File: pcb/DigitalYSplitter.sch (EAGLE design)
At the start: 42 parts, among them CN1 Battery, CON1 USB_MICROSMT+THRUHULE, CON2 M05X2NO_SILK, CON3 LED_OUT, CON5 LED_OUT, Q1 16MHz, SW1 BUTTON_1, SW2 BUTTON_2, U1 MK20D--VFM5, U3 74LVC1G17DCK, U4 74LVC1G17DCK, U5 74LVC1G17DCK, U6 TPD4S012, U7 74LVC1G17DCK

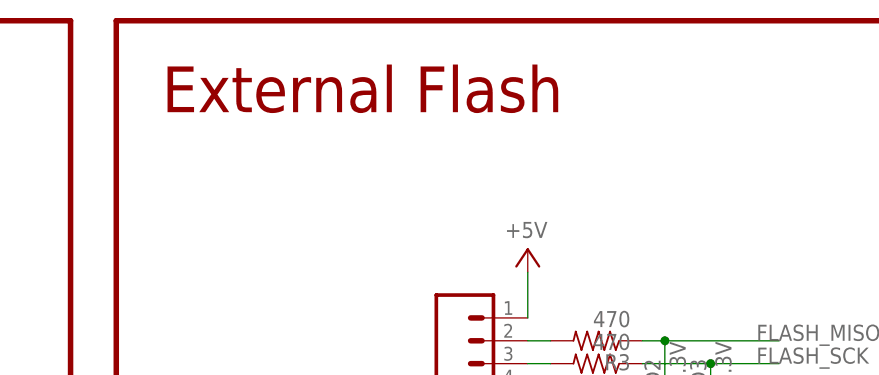
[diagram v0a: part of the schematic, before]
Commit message: Rename files, add .gitignore
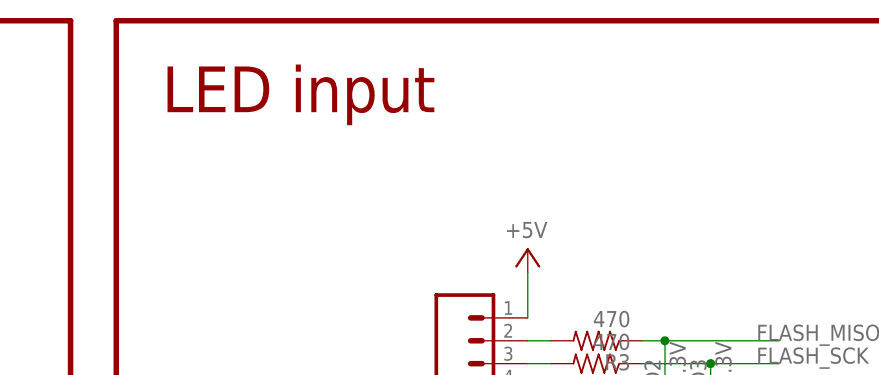
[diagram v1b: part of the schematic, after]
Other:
- note added: "LED input"
- note removed: "External Flash"
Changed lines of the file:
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@@
 <text x="20.32" y="238.76" size="5.08" layer="94">Processor</text>
 <wire x1="256.54" y1="248.92" x2="345.44" y2="248.92" width="0.6096" layer="94"/>
-<text x="261.62" y="238.76" size="5.08" layer="94">External Flash</text>
+<text x="261.62" y="238.76" size="5.08" layer="94">LED input</text>
 <wire x1="256.54" y1="248.92" x2="256.54" y2="165.1" width="0.6096" layer="94"/>
 <wire x1="345.44" y1="248.92" x2="345.44" y2="165.1" width="0.6096" layer="94"/>

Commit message: Small corrections to the PCB
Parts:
- removed LED5: STATUS, adafruit:LEDCHIPLED_0805
- removed R4: 470, adafruit:R-US_R0402
- renumbered LED6 to LED0
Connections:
- removed net N$16: LED1.A, R4.1
- removed net POWER_ENABLE: U1.PTD4
- removed net STATUS: LED1.C, U1.PTD6
- net +3V3: no longer R4.2
- net N$17: now also LED1.A; no longer LED5.A
- net TX: now also LED1.C; no longer LED5.C
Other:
- note removed: "Design Note: Signals POWER_ENABLE, STATUS, SW2, SW1 are GPIO and can be swapped to any other pin besides the ones on Port C"
- note removed: "Design Note: This is a generic flash pinout, there are equivalent parts from Winbond, Spansion, etc. Use the hardware chip select function to avoid conflicting with the LED output DMA."
- moved on the sheet: LED1
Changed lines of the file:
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@@
 <part name="GND10" library="SparkFun-Aesthetics" deviceset="GND" device=""/>
 <part name="C1" library="adafruit" deviceset="C-US" device="C0402" value="100nF"/>
-<part name="R4" library="adafruit" deviceset="R-US_" device="R0402" value="470"/>
-<part name="LED1" library="adafruit" deviceset="LED" device="CHIPLED_0805" value="STATUS"/>
 <part name="GND12" library="supply1" deviceset="GND" device=""/>
-<part name="3V3" library="supply1" deviceset="+3V3" device=""/>
 <part name="P+9" library="supply1" deviceset="+5V" device=""/>
 <part name="C3" library="adafruit" deviceset="C-US" device="C0402" value="100nF"/>
@@
 <part name="3V5" library="supply1" deviceset="+3V3" device=""/>
 <part name="R9" library="adafruit" deviceset="R-US_" device="R0402" value="470"/>
-<part name="LED5" library="adafruit" deviceset="LED" device="CHIPLED_0805" value="STATUS"/>
+<part name="LED1" library="adafruit" deviceset="LED" device="CHIPLED_0805" value="STATUS"/>
 <part name="3V6" library="supply1" deviceset="+3V3" device=""/>
 <part name="R10" library="adafruit" deviceset="R-US_" device="R0402" value="470"/>
-<part name="LED6" library="adafruit" deviceset="LED" device="CHIPLED_0805" value="STATUS"/>
+<part name="LED0" library="adafruit" deviceset="LED" device="CHIPLED_0805" value="STATUS"/>
 <part name="3V7" library="supply1" deviceset="+3V3" device=""/>
 </parts>
@@
 <wire x1="251.46" y1="124.46" x2="251.46" y2="40.64" width="0.6096" layer="94"/>
 <text x="20.32" y="114.3" size="5.08" layer="94">Buttons</text>
-<text x="165.1" y="134.62" size="1.778" layer="91">Design Note:
-Signals POWER_ENABLE, STATUS, SW2, SW1
-are GPIO and can be swapped to any other
-pin besides the ones on Port C</text>
 <text x="22.86" y="132.08" size="1.778" layer="91">Design Note:
 TPD4S012 is an ESD supression circuit, and are
@@
 <wire x1="345.44" y1="104.14" x2="345.44" y2="40.64" width="0.6096" layer="94"/>
 <wire x1="256.54" y1="40.64" x2="345.44" y2="40.64" width="0.6096" layer="94"/>
-<text x="261.62" y="170.18" size="1.778" layer="91">Design Note:
-This is a generic flash pinout, there are
-equivalent parts from Winbond, Spansion, etc.
-Use the hardware chip select function to avoid
-conflicting with the LED output DMA.</text>
 <text x="261.62" y="45.72" size="1.778" layer="91">Design Note:
 Disconnect USB before connecting to external power
@@
 <instance part="GND10" gate="1" x="302.26" y="195.58"/>
 <instance part="C1" gate="G$1" x="66.04" y="215.9"/>
-<instance part="R4" gate="G$1" x="228.6" y="185.42" rot="R90"/>
-<instance part="LED1" gate="G$1" x="228.6" y="175.26"/>
 <instance part="GND12" gate="1" x="35.56" y="78.74"/>
-<instance part="3V3" gate="G$1" x="228.6" y="195.58" smashed="yes">
-<attribute name="VALUE" x="226.06" y="196.85" size="1.778" layer="96"/>
-</instance>
 <instance part="P+9" gate="1" x="116.84" y="226.06" smashed="yes">
 <attribute name="VALUE" x="114.3" y="227.33" size="1.778" layer="96"/>
@@
 </instance>
 <instance part="R9" gate="G$1" x="10.16" y="7.62" rot="R90"/>
-<instance part="LED5" gate="G$1" x="10.16" y="-2.54"/>
+<instance part="LED1" gate="G$1" x="10.16" y="-2.54"/>
 <instance part="3V6" gate="G$1" x="10.16" y="17.78" smashed="yes">
 <attribute name="VALUE" x="7.62" y="19.05" size="1.778" layer="96"/>
 </instance>
 <instance part="R10" gate="G$1" x="22.86" y="7.62" rot="R90"/>
-<instance part="LED6" gate="G$1" x="22.86" y="-2.54"/>
+<instance part="LED0" gate="G$1" x="22.86" y="-2.54"/>
 <instance part="3V7" gate="G$1" x="22.86" y="17.78" smashed="yes">
 <attribute name="VALUE" x="20.32" y="19.05" size="1.778" layer="96"/>
@@
 </net>
 <net name="+3V3" class="0">
-<segment>
-<pinref part="3V3" gate="G$1" pin="+3V3"/>
-<pinref part="R4" gate="G$1" pin="2"/>
-<wire x1="228.6" y1="193.04" x2="228.6" y2="190.5" width="0.1524" layer="91"/>
-</segment>
 <segment>
 <wire x1="66.04" y1="220.98" x2="81.28" y2="220.98" width="0.1524" layer="91"/>
@@
 </segment>
 <segment>
-<pinref part="LED6" gate="G$1" pin="C"/>
+<pinref part="LED0" gate="G$1" pin="C"/>
 <wire x1="22.86" y1="-7.62" x2="22.86" y2="-15.24" width="0.1524" layer="91"/>
 <label x="22.86" y="-15.24" size="1.778" layer="95" rot="R90"/>
@@
 </segment>
 <segment>
-<pinref part="LED5" gate="G$1" pin="C"/>
+<pinref part="LED1" gate="G$1" pin="C"/>
 <wire x1="10.16" y1="-7.62" x2="10.16" y2="-15.24" width="0.1524" layer="91"/>
 <label x="10.16" y="-15.24" size="1.778" layer="95" rot="R90"/>
@@
 </segment>
 </net>
-<net name="STATUS" class="0">
-<segment>
-<pinref part="LED1" gate="G$1" pin="C"/>
-<wire x1="228.6" y1="170.18" x2="228.6" y2="162.56" width="0.1524" layer="91"/>
-<pinref part="U1" gate="G$1" pin="PTD6"/>
-<wire x1="187.96" y1="162.56" x2="228.6" y2="162.56" width="0.1524" layer="91"/>
-<label x="195.58" y="162.56" size="1.778" layer="95"/>
-</segment>
-</net>
-<net name="N$16" class="0">
-<segment>
-<pinref part="R4" gate="G$1" pin="1"/>
-<pinref part="LED1" gate="G$1" pin="A"/>
-<wire x1="228.6" y1="180.34" x2="228.6" y2="177.8" width="0.1524" layer="91"/>
-</segment>
-</net>
 <net name="RESET" class="0">
 <segment>
@@
 </segment>
 </net>
-<net name="POWER_ENABLE" class="0">
-<segment>
-<pinref part="U1" gate="G$1" pin="PTD4"/>
-<wire x1="187.96" y1="167.64" x2="205.74" y2="167.64" width="0.1524" layer="91"/>
-<label x="195.58" y="167.64" size="1.778" layer="95"/>
-</segment>
-</net>
 <net name="PA4" class="0">
 <segment>
@@
 <segment>
 <pinref part="R9" gate="G$1" pin="1"/>
-<pinref part="LED5" gate="G$1" pin="A"/>
+<pinref part="LED1" gate="G$1" pin="A"/>
 <wire x1="10.16" y1="2.54" x2="10.16" y2="0" width="0.1524" layer="91"/>
 </segment>
@@
 <segment>
 <pinref part="R10" gate="G$1" pin="1"/>
-<pinref part="LED6" gate="G$1" pin="A"/>
+<pinref part="LED0" gate="G$1" pin="A"/>
 <wire x1="22.86" y1="2.54" x2="22.86" y2="0" width="0.1524" layer="91"/>
 </segment>

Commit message: Small fixes to the PCB for clarity
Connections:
- net FLASH_MOSI renamed INPUT_MOSI
- new net INPUT_MISO: U1.PTC7
- new net INPUT_SCK: U1.PTC5
- net FLASH_MISO: no longer U1.PTC7
- net FLASH_SCK: no longer U1.PTC5
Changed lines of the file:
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@@
 <pinref part="R5" gate="G$1" pin="1"/>
 </segment>
-<segment>
-<pinref part="U1" gate="G$1" pin="PTC5"/>
-<wire x1="187.96" y1="180.34" x2="205.74" y2="180.34" width="0.1524" layer="91"/>
-<label x="195.58" y="180.34" size="1.778" layer="95"/>
-</segment>
-</net>
-<net name="FLASH_MOSI" class="0">
+</net>
+<net name="INPUT_MOSI" class="0">
 <segment>
 <pinref part="U1" gate="G$1" pin="PTC6"/>
@@
 <pinref part="R3" gate="G$1" pin="1"/>
 </segment>
-<segment>
-<pinref part="U1" gate="G$1" pin="PTC7"/>
-<wire x1="187.96" y1="175.26" x2="205.74" y2="175.26" width="0.1524" layer="91"/>
-<label x="195.58" y="175.26" size="1.778" layer="95"/>
-</segment>
 </net>
 <net name="RESET" class="0">
@@
 </segment>
 </net>
+<net name="INPUT_SCK" class="0">
+<segment>
+<pinref part="U1" gate="G$1" pin="PTC5"/>
+<wire x1="187.96" y1="180.34" x2="205.74" y2="180.34" width="0.1524" layer="91"/>
+<label x="195.58" y="180.34" size="1.778" layer="95"/>
+</segment>
+</net>
+<net name="INPUT_MISO" class="0">
+<segment>
+<pinref part="U1" gate="G$1" pin="PTC7"/>
+<wire x1="187.96" y1="175.26" x2="205.74" y2="175.26" width="0.1524" layer="91"/>
+<label x="195.58" y="175.26" size="1.778" layer="95"/>
+</segment>
+</net>
